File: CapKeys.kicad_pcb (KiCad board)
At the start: 2 copper layers, 137 parts, among them J1 USB_C_Receptacle_USB2.0_16P, J10 Conn_01x01, J11 Conn_01x01, J12 Conn_01x01, J13 Conn_01x01, J14 Conn_01x01, J15 Conn_01x01, J16 Conn_01x01, J17 Conn_01x01, J18 Conn_01x01, J19 Conn_01x01, J2 Conn_01x01, J20 Conn_01x01, J21 Conn_01x01, J22 Conn_01x01, J23 Conn_01x01, J24 Conn_01x01, J25 Conn_01x01, J26 Conn_01x01, J27 Conn_01x01, J28 Conn_01x01, J29 Conn_01x01, J3 Conn_01x01, J30 Conn_01x01, J31 Conn_01x01, J32 Conn_01x01, J33 Conn_01x01, J34 Conn_01x01, J35 Conn_01x01, J36 Conn_01x01, J37 Conn_01x01, J38 Conn_01x01, J39 Conn_01x01, J4 Conn_01x01, J40 Conn_01x01, J41 Conn_01x01, J42 Conn_01x01, J43 Conn_01x01, J44 Conn_01x01, J45 Conn_01x01, J46 Conn_01x01, J47 Conn_01x01, J5 Conn_01x01, J6 Conn_01x01, J7 Conn_01x01, J8 Conn_01x01, J9 Conn_01x01, U1 W25Q128JVS, U2 MPR121QR2, U3 AMS1117-3.3, U4 MPR121QR2, U5 MPR121QR2, U6 MPR121QR2, U7 RP2040, Y1 X322512MSB4SI

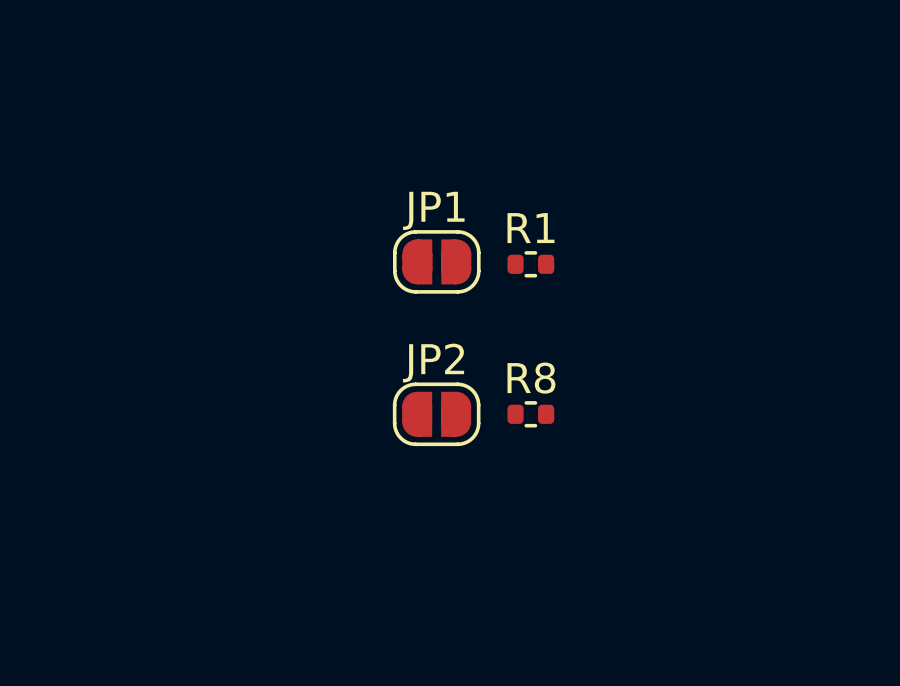
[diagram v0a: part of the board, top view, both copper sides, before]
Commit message: Updated symbols and footprints
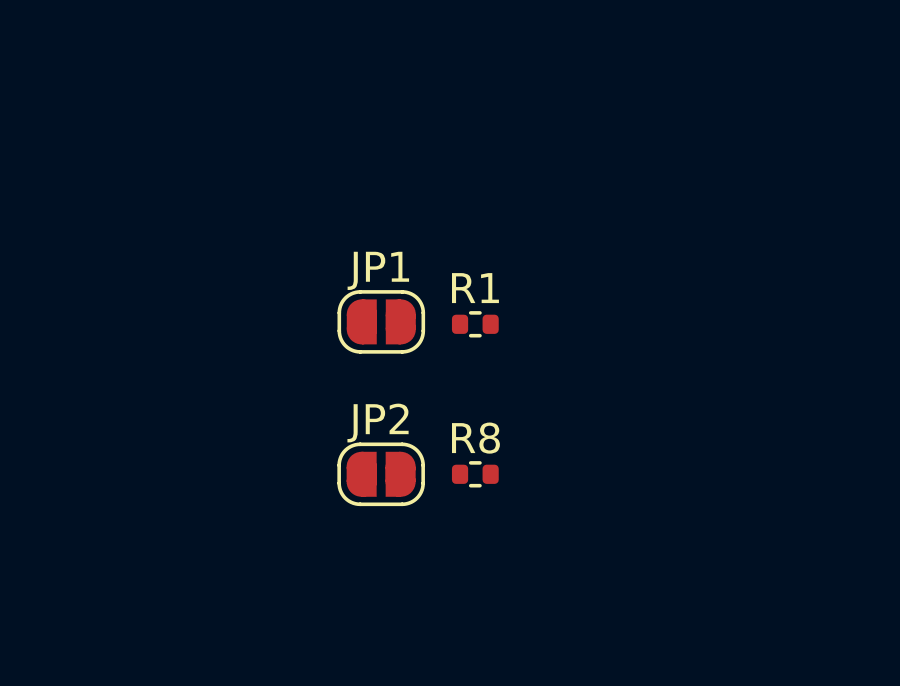
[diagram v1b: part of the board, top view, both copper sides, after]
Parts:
- moved R1 2.72 mm to (126.6, 130.6)
- moved R8 2.72 mm to (126.6, 135.6)
- moved JP1 2.72 mm to (123.5, 130.5)
- moved JP2 2.72 mm to (123.5, 135.6)
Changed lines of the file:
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@@
 	(footprint "Jumper:SolderJumper-2_P1.3mm_Open_RoundedPad1.0x1.5mm"
 		(layer "F.Cu")
-		(at 125.345 133.58)
+		(at 123.495 135.58)
 		(descr "SMD Solder Jumper, 1x1.5mm, rounded Pads, 0.3mm gap, open")
 		(tags "solder jumper open")
@@
 	(footprint "Resistor_SMD:R_0402_1005Metric"
 		(layer "F.Cu")
-		(at 128.485 133.58)
+		(at 126.635 135.58)
 		(descr "Resistor SMD 0402 (1005 Metric), square (rectangular) end terminal, IPC-7351 nominal, (Body size source: IPC-SM-782 page 72, https://www.pcb-3d.com/wordpress/wp-content/uploads/ipc-sm-782a_amendment_1_and_2.pdf)")
 		(tags "resistor")
@@
 	(footprint "Resistor_SMD:R_0402_1005Metric"
 		(layer "F.Cu")
-		(at 128.485 128.58)
+		(at 126.635 130.58)
 		(descr "Resistor SMD 0402 (1005 Metric), square (rectangular) end terminal, IPC-7351 nominal, (Body size source: IPC-SM-782 page 72, https://www.pcb-3d.com/wordpress/wp-content/uploads/ipc-sm-782a_amendment_1_and_2.pdf)")
 		(tags "resistor")
@@
 	(footprint "Jumper:SolderJumper-2_P1.3mm_Open_RoundedPad1.0x1.5mm"
 		(layer "F.Cu")
-		(at 125.35 128.5)
+		(at 123.5 130.5)
 		(descr "SMD Solder Jumper, 1x1.5mm, rounded Pads, 0.3mm gap, open")
 		(tags "solder jumper open")

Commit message: Updated footprints,symbols,and PCB
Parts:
- removed J10, J11, J12, J16, J17, J18, J27, J28, J29, J33, J34, J35, J39, J40, J41: Conn_01x01, Footprints:KEY_BLACK
- removed J13, J14, J15, J2, J21, J22, J23, J24, J25, J26, J3, J30, J31, J32, J36, J37, J38, J4, J42, J43, J44, J45, J46, J47: Conn_01x01, Footprints:KEY_WHITE
- removed J5, J6, J7, J8, J9: Conn_01x01, Footprints:KEY_OTHER
- added H1: MountingHole, MountingHole:MountingHole_3.2mm_M3, F.Cu at (95.0, 82.0)
- added H2: MountingHole, MountingHole:MountingHole_3.2mm_M3, F.Cu at (95.0, 90.0)
- added H3: MountingHole, MountingHole:MountingHole_3.2mm_M3, F.Cu at (103.0, 82.0)
- added H4: MountingHole, MountingHole:MountingHole_3.2mm_M3, F.Cu at (103.0, 90.0)
- added H5: MountingHole, MountingHole:MountingHole_3.2mm_M3, F.Cu at (110.9, 82.0)
- added H6: MountingHole, MountingHole:MountingHole_3.2mm_M3, F.Cu at (110.9, 90.0)
- added U8: ~, Footprints:KEYS, F.Cu at (220.1, 198.8)
- added U9: ~, Footprints:PTB_KEYS, F.Cu at (119.5, 180.4)
- C6, C7: footprint Capacitor_SMD:C_0402_1005Metric -> Capacitor_SMD:C_1206_3216Metric
- D1, D10, D11, D12, D13, D14, D15, D16, D17, D18, D19, D2, D20, D21, D3, D4, D5, D6, D7, D8, D9: value GL0805YG01 -> P2-0805G2TS2-08T-002
- moved D17 200.8 mm to (150.4, 67.0)
- moved D13 187.0 mm to (145.9, 76.1)
- moved D18 183.0 mm to (150.4, 70.0)
- moved R23 181.6 mm to (149.4, 83.6)
- moved R28 174.4 mm to (149.4, 93.6)
- moved R29 171.8 mm to (152.3, 81.6)
- moved D12 171.5 mm to (145.9, 73.0)
- moved D19 165.3 mm to (150.4, 73.0)
- moved R22 164.8 mm to (149.4, 81.6)
- moved R7 164.7 mm to (127.3, 114.8), turned to 90 degrees
- moved D10 161.0 mm to (145.9, 67.0)
- moved J1 160.3 mm to (126.0, 108.3)
- moved R4 155.7 mm to (124.3, 114.7), turned to 90 degrees
- moved R30 155.2 mm to (152.3, 83.6)
- moved D8 154.1 mm to (145.9, 60.9)
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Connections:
- D14 pad 1: /LED_OCT3 -> GND
- D15 pad 1: /LED_OCT2 -> GND
- D16 pad 1: /LED_OCT1 -> GND
- D17 pad 1: /LED_PTB-2 -> GND
- D18 pad 1: /LED_PTB-1 -> GND
- D19 pad 1: /LED_PTB0 -> GND
- D20 pad 1: /LED_PTB+1 -> GND
- D21 pad 1: /LED_PTB+2 -> GND
- R25 pad 2: +3V3 -> /LED_PTB+2
- R26 pad 2: +3V3 -> /LED_PTB+1
- R27 pad 2: +3V3 -> /LED_PTB0
- R28 pad 2: +3V3 -> /LED_PTB-1
- R29 pad 2: +3V3 -> /LED_PTB-2
- R30 pad 2: +3V3 -> /LED_OCT1
- R31 pad 2: +3V3 -> /LED_OCT2
- R32 pad 2: +3V3 -> /LED_OCT3
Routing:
- added copper zone on B.Cu, net GND
- added copper zone on F.Cu, net GND
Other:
- board outline added: 215 x 130 mm

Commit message: Updated PCB and schematic
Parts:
- moved D13 173.7 mm to (294.0, 167.0), turned to 180 degrees
- moved R23 164.7 mm to (291.5, 167.0), turned to 90 degrees
- moved D12 162.0 mm to (277.9, 167.0), turned to 180 degrees
- moved D18 155.5 mm to (132.6, 224.5)
- moved R22 152.3 mm to (275.5, 167.0), turned to 90 degrees
- moved D11 148.2 mm to (265.5, 157.5), turned to 180 degrees
- moved D17 147.6 mm to (132.5, 213.5)
- moved D10 146.9 mm to (253.6, 167.0), turned to 180 degrees
- moved R29 143.9 mm to (135.0, 224.5), turned to 90 degrees
- moved D16 139.7 mm to (132.5, 202.5)
- moved U6 136.6 mm to (262.6, 131.0)
- moved D8 135.4 mm to (230.1, 167.0), turned to 180 degrees
- moved D9 134.1 mm to (242.0, 157.5), turned to 180 degrees
- moved R21 132.9 mm to (263.0, 157.5), turned to 90 degrees
- moved D15 131.8 mm to (132.6, 191.5)
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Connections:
- U2 pad 10: /KEY_D_1 -> /KEY_PTB0
- U2 pad 11: /KEY_D#_1 -> /KEY_PTB+1
- U2 pad 12: /KEY_E_1 -> /KEY_PTB+2
- U2 pad 13: /KEY_F_1 -> /KEY_PTB-1
- U2 pad 14: /KEY_F#_1 -> /KEY_PTB-2
- U2 pad 15: /KEY_G_1 -> /KEY_C_1
- U2 pad 16: /KEY_G#_1 -> /KEY_C_2
- U2 pad 17: /KEY_A_1 -> /KEY_C_3
- U2 pad 18: /KEY_A#_1 -> /KEY_C#_1
- U2 pad 19: /KEY_B_1 -> /KEY_C#_2
- U2 pad 8: /KEY_C_1 -> /KEY_OCT+
- U2 pad 9: /KEY_C#_1 -> /KEY_OCT-
- U4 pad 11: /KEY_D#_2 -> /KEY_D_3
- U4 pad 12: /KEY_E_2 -> /KEY_D#_1
- U4 pad 13: /KEY_F_2 -> /KEY_D#_2
- U4 pad 14: /KEY_F#_2 -> /KEY_D#_3
- U4 pad 15: /KEY_G_2 -> /KEY_E_1
- U4 pad 16: /KEY_G#_2 -> /KEY_E_2
- U4 pad 17: /KEY_A_2 -> /KEY_E_3
- U4 pad 18: /KEY_A#_2 -> /KEY_F_1
- U4 pad 19: /KEY_B_2 -> /KEY_F_2
- U4 pad 8: /KEY_C_2 -> /KEY_C#_3
- U4 pad 9: /KEY_C#_2 -> /KEY_D_1
- U5 pad 10: /KEY_D_3 -> /KEY_F#_2
- U5 pad 11: /KEY_D#_3 -> /KEY_F#_3
- U5 pad 12: /KEY_E_3 -> /KEY_G_1
- U5 pad 13: /KEY_F_3 -> /KEY_G_2
- U5 pad 14: /KEY_F#_3 -> /KEY_G_3
- U5 pad 15: /KEY_G_3 -> /KEY_G#_1
- U5 pad 16: /KEY_G#_3 -> /KEY_G#_2
- U5 pad 17: /KEY_A_3 -> /KEY_G#_3
- U5 pad 18: /KEY_A#_3 -> /KEY_A_1
- U5 pad 19: /KEY_B_3 -> /KEY_A_2
- U5 pad 8: /KEY_C_3 -> /KEY_F_3
- U5 pad 9: /KEY_C#_3 -> /KEY_F#_1
- U6 pad 10: /KEY_HC_3 -> /KEY_A#_2
- U6 pad 11: /KEY_OCT+ -> /KEY_A#_3
- U6 pad 12: /KEY_OCT- -> /KEY_B_1
- U6 pad 13: /KEY_PTB0 -> /KEY_B_2
- U6 pad 14: /KEY_PTB+1 -> /KEY_B_3
- U6 pad 15: /KEY_PTB+2 -> /KEY_HC_1
- U6 pad 16: /KEY_PTB-1 -> /KEY_HC_2
- U6 pad 17: /KEY_PTB-2 -> /KEY_HC_3
- U6 pad 18: /KEY_MUTE -> unconnected-(U6-ELEC10-Pad18)
- U6 pad 8: /KEY_HC_1 -> /KEY_A_3
- U6 pad 9: /KEY_HC_2 -> /KEY_A#_1
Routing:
- net /USB_D+: track 0.00 -> 46.3 mm
- net /USB_D-: track 0.00 -> 45.3 mm
- net GND: track 0.00 -> 22.7 mm, vias 0 -> 27
- net Net-(U6-VREG): track 0.00 -> 1.71 mm
- added copper zone on F.Cu, net +3V3

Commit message: Updated PCB
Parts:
- moved JP1 25.9 mm to (146.3, 119.5)
- moved R1 25.9 mm to (146.3, 117.4), turned to 0 degrees
- moved R5 11.9 mm to (150.3, 124.1), turned to 180 degrees
- moved R3 5.04 mm to (150.3, 122.5), turned to 180 degrees
- moved C4 4.02 mm to (156.2, 130.5)
- moved Y1 4.02 mm to (154.6, 132.8)
- moved R2 4.00 mm to (150.3, 121.5), turned to 180 degrees
- moved C1 3.98 mm to (149.9, 110.2)
- moved U1 2.79 mm to (153.4, 113.8), turned to 90 degrees
- moved R10 2.32 mm to (154.9, 136.2), turned to 0 degrees
- moved C5 2.30 mm to (152.9, 136.2), turned to 0 degrees
- moved R24 1.75 mm to (223.1, 134.6)
- moved C11 1.75 mm to (222.6, 128.3)
- moved C10 1.75 mm to (221.4, 133.1)
- moved U5 1.75 mm to (224.3, 131.4)
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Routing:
- net /~{IRQ}: track 0.00 -> 158.2 mm
- net /SCL: track 0.00 -> 149.7 mm, vias 0 -> 4
- net +3V3: track 0.00 -> 97.6 mm, vias 0 -> 21
- net /SDA: track 0.00 -> 73.8 mm
- net VBUS: track 0.00 -> 68.1 mm
- net /LED_OCT1: track 0.00 -> 40.7 mm, vias 0 -> 2
- net /LED_OCT2: track 0.00 -> 36.9 mm, vias 0 -> 3
- net /LED_OCT3: track 0.00 -> 33.5 mm, vias 0 -> 2
- net /QSPI_SD3: track 0.00 -> 16.3 mm
- net +1V1: track 0.00 -> 16.0 mm
- net /QSPI_SCLK: track 0.00 -> 13.9 mm
- net GND: track 22.7 -> 35.3 mm, vias 27 -> 49
- net /XOUT: track 0.00 -> 12.4 mm
- net /~{QSPI_SS}: track 0.00 -> 11.4 mm
- net /QSPI_SD0: track 0.00 -> 10.8 mm
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- added copper zone on B.Cu, net +3V3

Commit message: Updated PCB and Footprints
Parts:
- moved R7 0.37 mm to (132.8, 111.7)
- moved U9 0.19 mm to (119.5, 180.6)
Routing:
- net /~{IRQ}: track 158.2 -> 7.05 mm
- net /SCL: track 149.7 -> 6.55 mm, vias 4 -> 0
- net +3V3: track 97.6 -> 8.33 mm, vias 21 -> 2
- net /SDA: track 73.8 -> 6.30 mm
- net /LED_OCT1: track 40.7 -> 0.00 mm, vias 2 -> 0
- net /LED_OCT2: track 36.9 -> 0.00 mm, vias 3 -> 0
- net /LED_OCT3: track 33.5 -> 0.00 mm, vias 2 -> 0
- net GND: track 35.3 -> 16.2 mm, vias 49 -> 35
- net VBUS: track 68.1 -> 85.9 mm
- net /XOUT: track 12.4 -> 0.00 mm
- net /XIN: track 8.39 -> 0.00 mm
- net Net-(J1-CC2): track 0.00 -> 6.21 mm
- net /RUN: track 7.76 -> 1.76 mm
- net Net-(C5-Pad2): track 3.56 -> 0.00 mm
- net +1V1: track 16.0 -> 18.1 mm
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- added copper zone on In2.Cu, net +3V3
- added copper zone on In1.Cu, net GND
- removed copper zone on B.Cu, net +3V3
- removed copper zone on B.Cu, net GND
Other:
- copper layers 2 -> 4

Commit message: Updated PCB and Footprints
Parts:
- moved U8 0.14 mm to (219.9, 199.2)
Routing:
- net /LED_HC: track 0.00 -> 150.3 mm
- net /LED_B: track 0.00 -> 132.6 mm
- net /LED_A#: track 0.00 -> 115.0 mm
- net /LED_PTB0: track 0.00 -> 110.1 mm, vias 0 -> 2
- net /LED_G#: track 0.00 -> 109.8 mm, vias 0 -> 2
- net /LED_A: track 0.00 -> 108.1 mm
- net /LED_PTB-1: track 0.00 -> 100.5 mm, vias 0 -> 2
- net /LED_G: track 0.00 -> 84.6 mm
- net /LED_PTB+1: track 0.00 -> 81.3 mm, vias 0 -> 2
- net /LED_PTB+2: track 0.00 -> 72.0 mm, vias 0 -> 2
- net /LED_F#: track 0.00 -> 65.3 mm
- net /LED_F: track 0.00 -> 58.3 mm
- net /LED_D#: track 0.00 -> 57.4 mm
- net /LED_D: track 0.00 -> 53.8 mm
- net /LED_E: track 0.00 -> 53.6 mm
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
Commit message: Updated PCB
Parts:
- moved U8 0.20 mm to (219.9, 199.4)
- moved U9 0.10 mm to (119.5, 180.7)
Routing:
- net /LED_PTB0: track 110.1 -> 105.1 mm
- net /LED_D#: track 57.4 -> 62.2 mm
- net GND: track 29.4 -> 33.1 mm, vias 48 -> 81
- net /LED_PTB-1: vias 2 -> 3

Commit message: Updated PCB
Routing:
- net /SDA: track 6.30 -> 193.3 mm, vias 0 -> 5
- net /~{IRQ}: track 7.15 -> 183.9 mm, vias 0 -> 6
- net /SCL: track 6.55 -> 183.2 mm, vias 0 -> 6
- net /KEY_PTB-2: track 0.00 -> 71.4 mm, vias 0 -> 2
- net /KEY_C_1: track 0.00 -> 65.0 mm, vias 0 -> 2
- net /KEY_PTB-1: track 0.00 -> 63.6 mm, vias 0 -> 2
- net /KEY_C_2: track 0.00 -> 57.0 mm, vias 0 -> 2
- net /KEY_C#_1: track 0.00 -> 49.5 mm, vias 0 -> 2
- net /KEY_PTB0: track 0.00 -> 42.0 mm, vias 0 -> 2
- net +3V3: track 33.9 -> 70.7 mm
- net /KEY_PTB+1: track 0.00 -> 34.8 mm, vias 0 -> 2
- net /KEY_C#_2: track 0.00 -> 32.3 mm, vias 0 -> 2
- net /KEY_OCT+: track 0.00 -> 30.6 mm, vias 0 -> 2
- net /KEY_OCT-: track 0.00 -> 27.3 mm, vias 0 -> 2
- net /KEY_PTB+2: track 0.00 -> 23.8 mm, vias 0 -> 2
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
